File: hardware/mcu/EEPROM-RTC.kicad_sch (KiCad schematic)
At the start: 11 parts, among them U2 M24C04, U4 MAX31331TET, Y2 Crystal

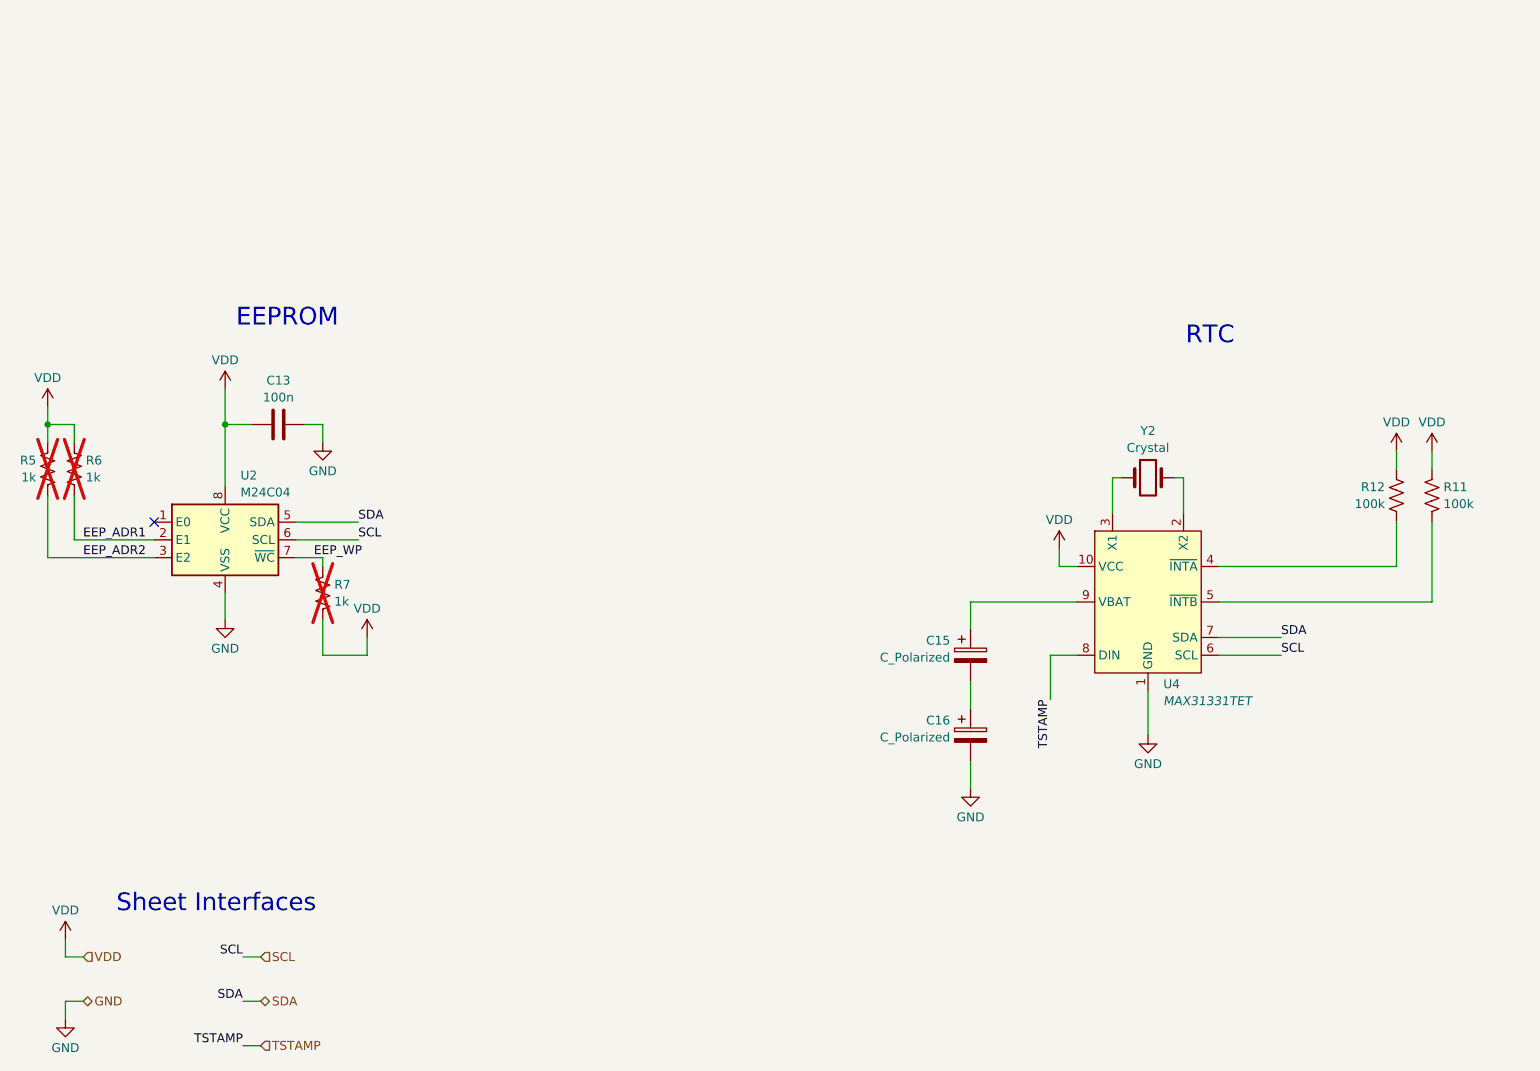
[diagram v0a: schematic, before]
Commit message: I2C device notes
added notes on I2C device addresses (in-schematic)
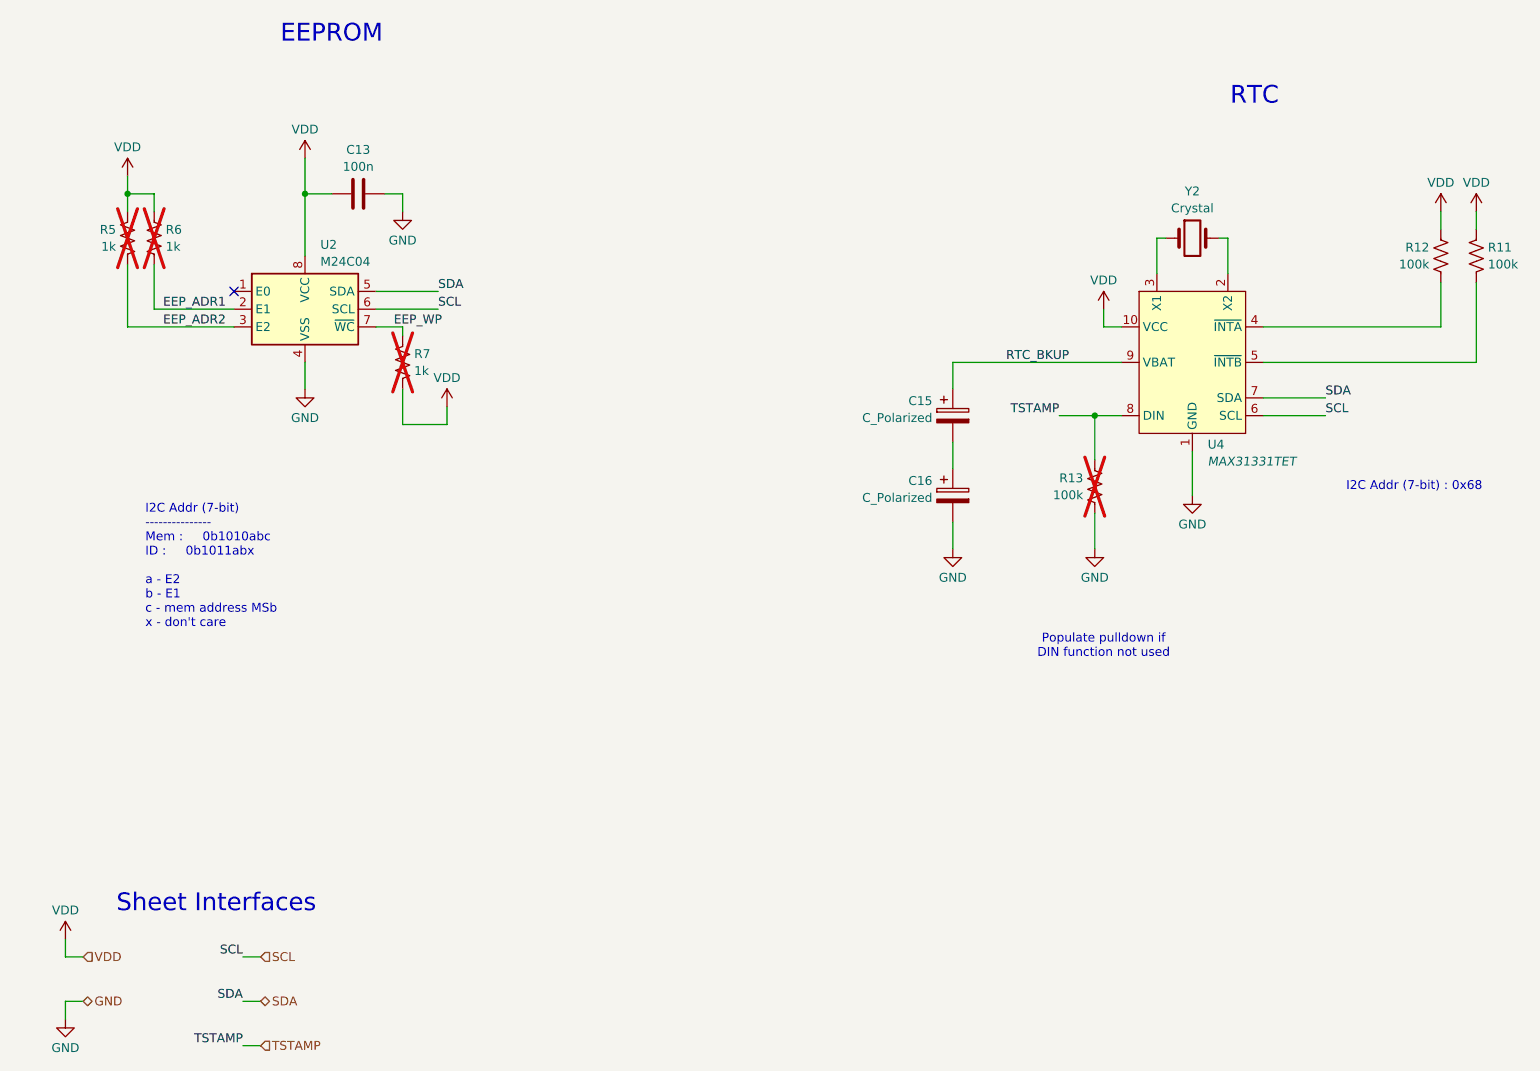
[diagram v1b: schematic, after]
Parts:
- added R13: 100k, Resistor_SMD:R_0402_1005Metric_Pad0.72x0.64mm_HandSolder, symbol Device:R_US
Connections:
- net GND: now also R13.1
- net TSTAMP: now also R13.2
- net RTC_BKUP: now reaches C15.1, U4.9 (VBAT)
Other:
- note added: "I2C Addr (7-bit) --------------- Mem : 0b1010abc ID : 0b1011abx a - E2 b - E1 c - mem address MSb x - don't care"
- note added: "I2C Addr (7-bit) : 0x68"
- note added: "Populate pulldown if DIN function not used"
- moved on the sheet: C13, C15, C16, R11, R12, R5, R6, R7, U2, U4, Y2
